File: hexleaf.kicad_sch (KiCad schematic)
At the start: 42 parts, among them IC1 ESP32-C3-FH4, J2 Conn_01x04, J5 Conn_01x08, J6 Conn_01x04, J7 Conn_01x08, SW1 SW_SPST, SW2 SW_SPST, Y1 ECS-400-10-37B2-CKM-TR

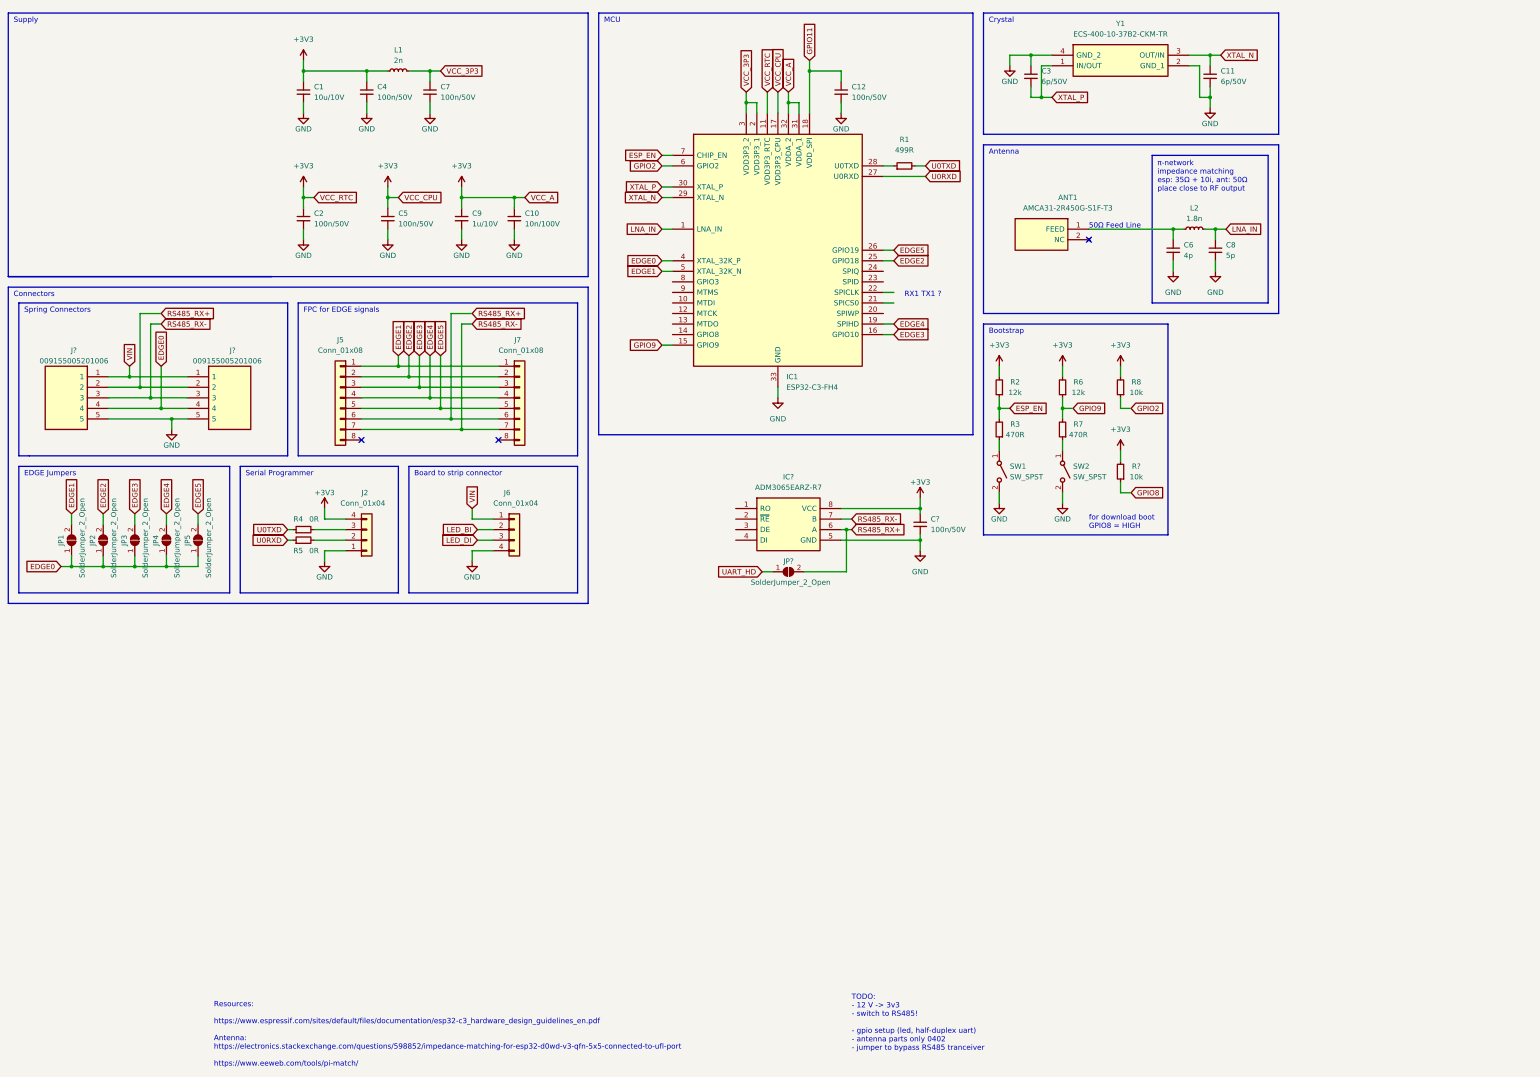
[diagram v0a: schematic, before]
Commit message: redone gpio0 labels + added rs485 pins
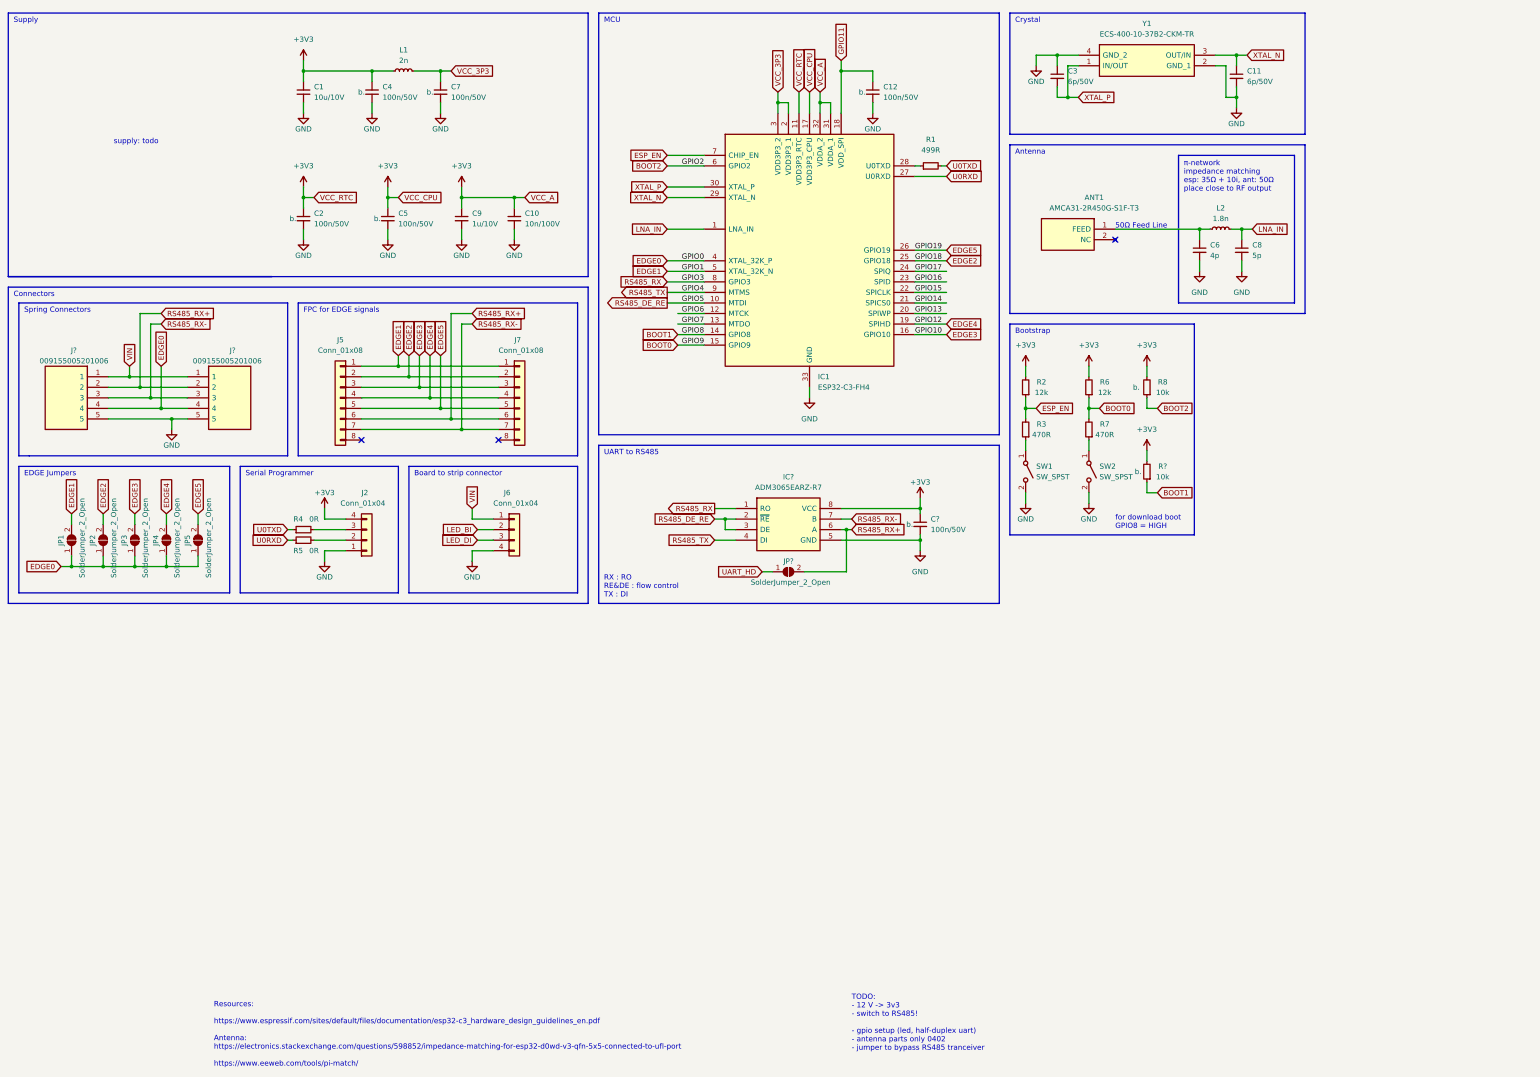
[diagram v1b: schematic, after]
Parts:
- C12, C2, C4, C5, C7, C?, R8, R?: in stock (none) -> b.
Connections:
- net GPIO8 is gone; now on net BOOT1: R?.1
- net RS485_DE_RE: now reaches IC1.10 (MTDI)
- net RS485_DE_RE: now also IC?.2 (~{RE}), IC?.3 (DE)
- net GPIO6: now reaches IC1.12 (MTCK)
- net GPIO7: now reaches IC1.13 (MTDO)
- net BOOT1: now reaches IC1.14 (GPIO8)
- net GPIO13: now reaches IC1.20 (SPIWP)
- net GPIO14: now reaches IC1.21 (SPICS0)
- net GPIO15: now reaches IC1.22 (SPICLK)
- net GPIO16: now reaches IC1.23 (SPID)
- net GPIO17: now reaches IC1.24 (SPIQ)
- net RS485_RX: now reaches IC1.8 (GPIO3)
- net RS485_RX: now also IC?.1 (RO)
- net RS485_TX: now reaches IC1.9 (MTMS)
- net RS485_TX: now also IC?.4 (DI)
- net GPIO2 renamed BOOT2
- net GPIO9 renamed BOOT0
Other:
- note added: "RX : RO RE&DE : flow control TX : DI"
- note added: "UART to RS485"
- note added: "supply: todo"
- note removed: "RX1 TX1 ?"
- moved on the sheet: ANT1, C11, C12, C3, C4, C6, C7, C8, IC1, L1, L2, R1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

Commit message: led pins and RS485 bypass jumper
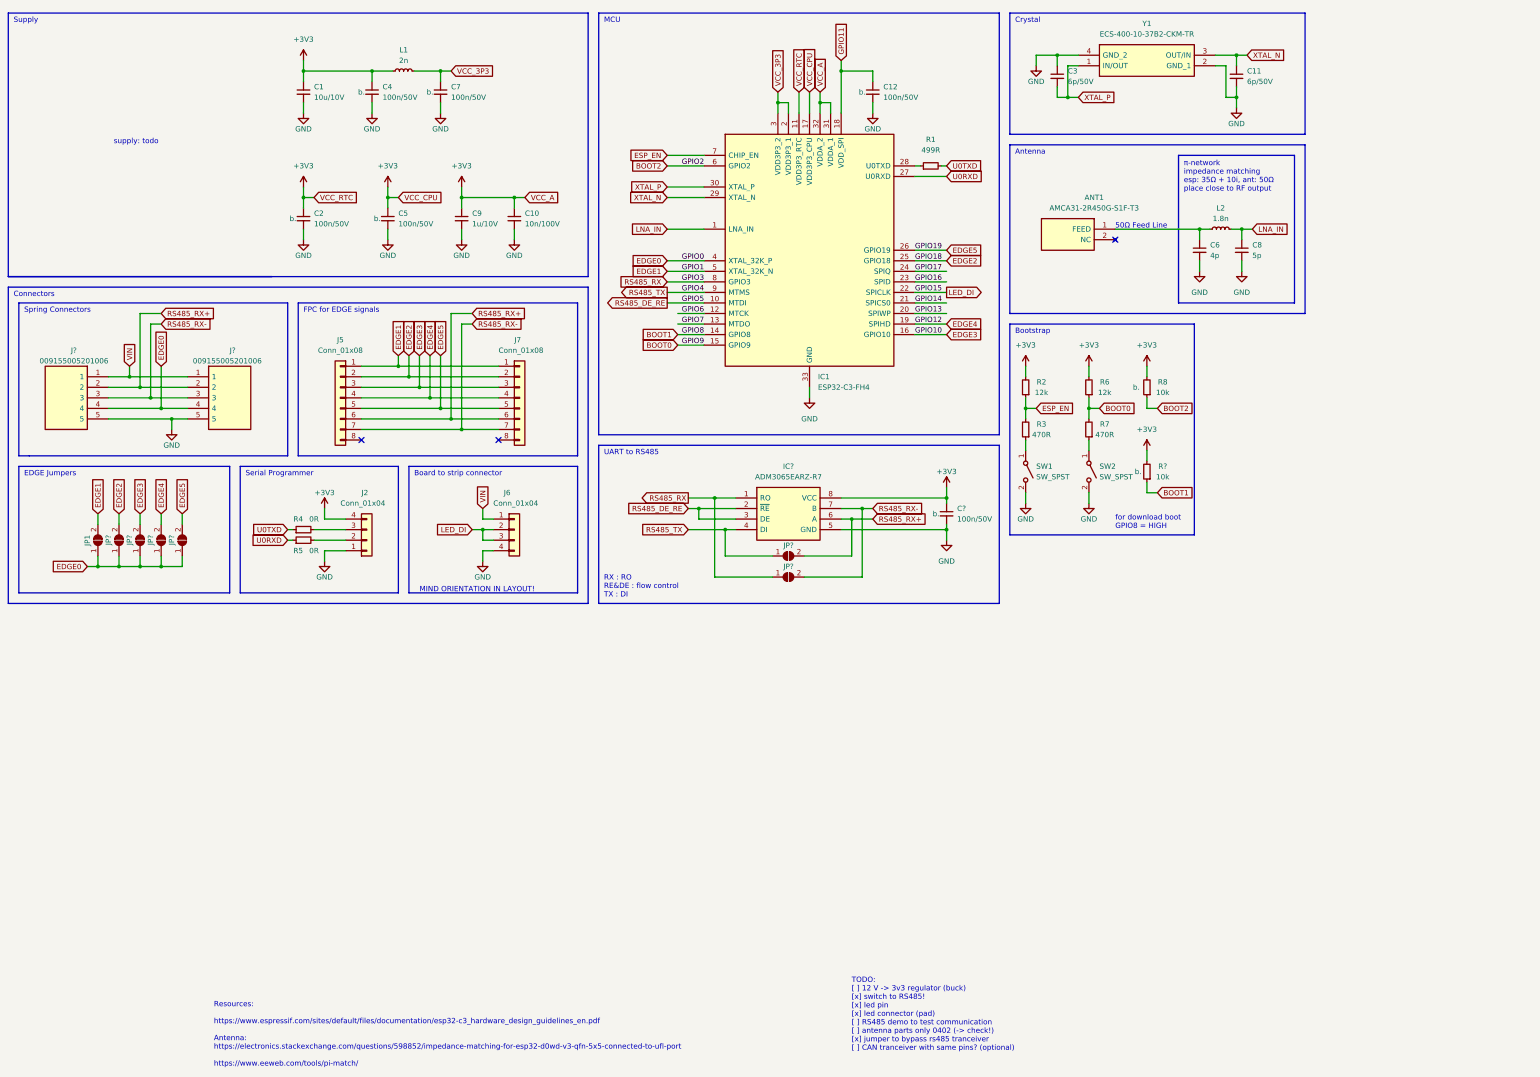
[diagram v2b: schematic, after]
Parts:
- removed JP2, JP3, JP4, JP5: SolderJumper_2_Open, Jumper:SolderJumper-2_P1.3mm_Open_TrianglePad1.0x1.5mm, symbol Jumper:SolderJumper_2_Open
- added JP? (x5): SolderJumper_2_Open, Jumper:SolderJumper-2_P1.3mm_Open_TrianglePad1.0x1.5mm, symbol Jumper:SolderJumper_2_Open
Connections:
- net GPIO15 is gone; now on net LED_DI: IC1.22 (SPICLK)
- net LED_BI is gone; now on net LED_DI: J6.2 (Pin_2)
- net UART_HD is gone; now on net RS485_TX: JP?.1 (A)
- net EDGE0: now also JP?.1 (A), JP?.1 (A), JP?.1 (A), JP?.1 (A)
- net EDGE2: now also JP?.2 (B)
- net EDGE3: now also JP?.2 (B)
- net EDGE4: now also JP?.2 (B)
- net EDGE5: now also JP?.2 (B)
- net RS485_RX: now also JP?.1 (A)
- net RS485_RX-: now also JP?.2 (B)
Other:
- note added: "MIND ORIENTATION IN LAYOUT!"
- note added: "TODO: [ ] 12 V -> 3v3 regulator (buck) [x] switch to RS485! [x] led pin [x] led connector (pad) [ ] RS485 demo to test communication [ ] antenna parts only 0402 (-> check!) [x] jumper to bypass rs485 tranceiver [ ] CAN tranceiver with same pins? (optional)"
- note removed: "TODO: - 12 V -> 3v3 - switch to RS485! - gpio setup (led, half-duplex uart) - antenna parts only 0402 - jumper to bypass RS485 tranceiver"
- moved on the sheet: C?, IC?, JP1, JP?

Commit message: added buck
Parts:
- removed C10: 10n/100V, Resistor_SMD:R_0805_2012Metric, symbol Device:C_Small
- removed C2, C5: 100n/50V, Resistor_SMD:R_0603_1608Metric, symbol Device:C_Small
- removed C9: 1u/10V, Resistor_SMD:R_0603_1608Metric, symbol Device:C_Small
- added C? (x2): 22uF /10V, Capacitor_SMD:C_0603_1608Metric, symbol Device:C_Small
- added C? (x3): 100n/50V, Resistor_SMD:R_0603_1608Metric, symbol Device:C_Small
- added C?: 10n/100V, Resistor_SMD:R_0805_2012Metric, symbol Device:C_Small
- added C?: 10u/10V, Resistor_SMD:R_0805_2012Metric, symbol Device:C_Small
- added C?: 1u/10V, Resistor_SMD:R_0603_1608Metric, symbol Device:C_Small
- added L?: 2.2u, hexleaf:L_5024, symbol Device:L_Small
- added PS?: AP62301WU-7, hexleaf:SOT95P280X100-6N, symbol hexleaf:AP62301WU-7
- added R? (x2): DNF, Resistor_SMD:R_0402_1005Metric, symbol Device:R_Small
- added R?: 24k, Resistor_SMD:R_0402_1005Metric, symbol Device:R_Small
- added R?: 75k, Resistor_SMD:R_0402_1005Metric, symbol Device:R_Small
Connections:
- net +3V3: now also C?.1, C?.1, C?.1, C?.1, C?.1, C?.1, L?.2, R?.1
- net GND: now also C?.2, C?.2, C?.2, C?.2, C?.2, C?.2, C?.2, PS?.1 (GND), R?.2, R?.2
- net VIN: now also C?.1, PS?.3 (VIN), R?.1
- new net: C?.1, PS?.6 (BST)
- new net: C?.2, L?.1, PS?.2 (SW)
- new net: PS?.4 (FB), R?.1, R?.2
- new net: PS?.5 (EN), R?.1, R?.2
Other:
- note added: "ESP32"
- note added: "GPIO11 supply for internal flash"
- note added: "MCU supply"
- note added: "Main Supply 12V -> 3v3 BUCK Vin 4.2 - 18V, Vout 0.8 - 7V"
- note removed: "MCU"
- note removed: "Supply"
- note removed: "supply: todo"
- moved on the sheet: ANT1, C1, C11, C12, C3, C4, C6, C7, C8, C?, IC1, IC?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
